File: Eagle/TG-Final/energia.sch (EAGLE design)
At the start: 55 parts, among them IC1 7812T, IC2 7805, IC3 AZ1117, IC4 7806T, Q1 TIP2955, T1 2N3904

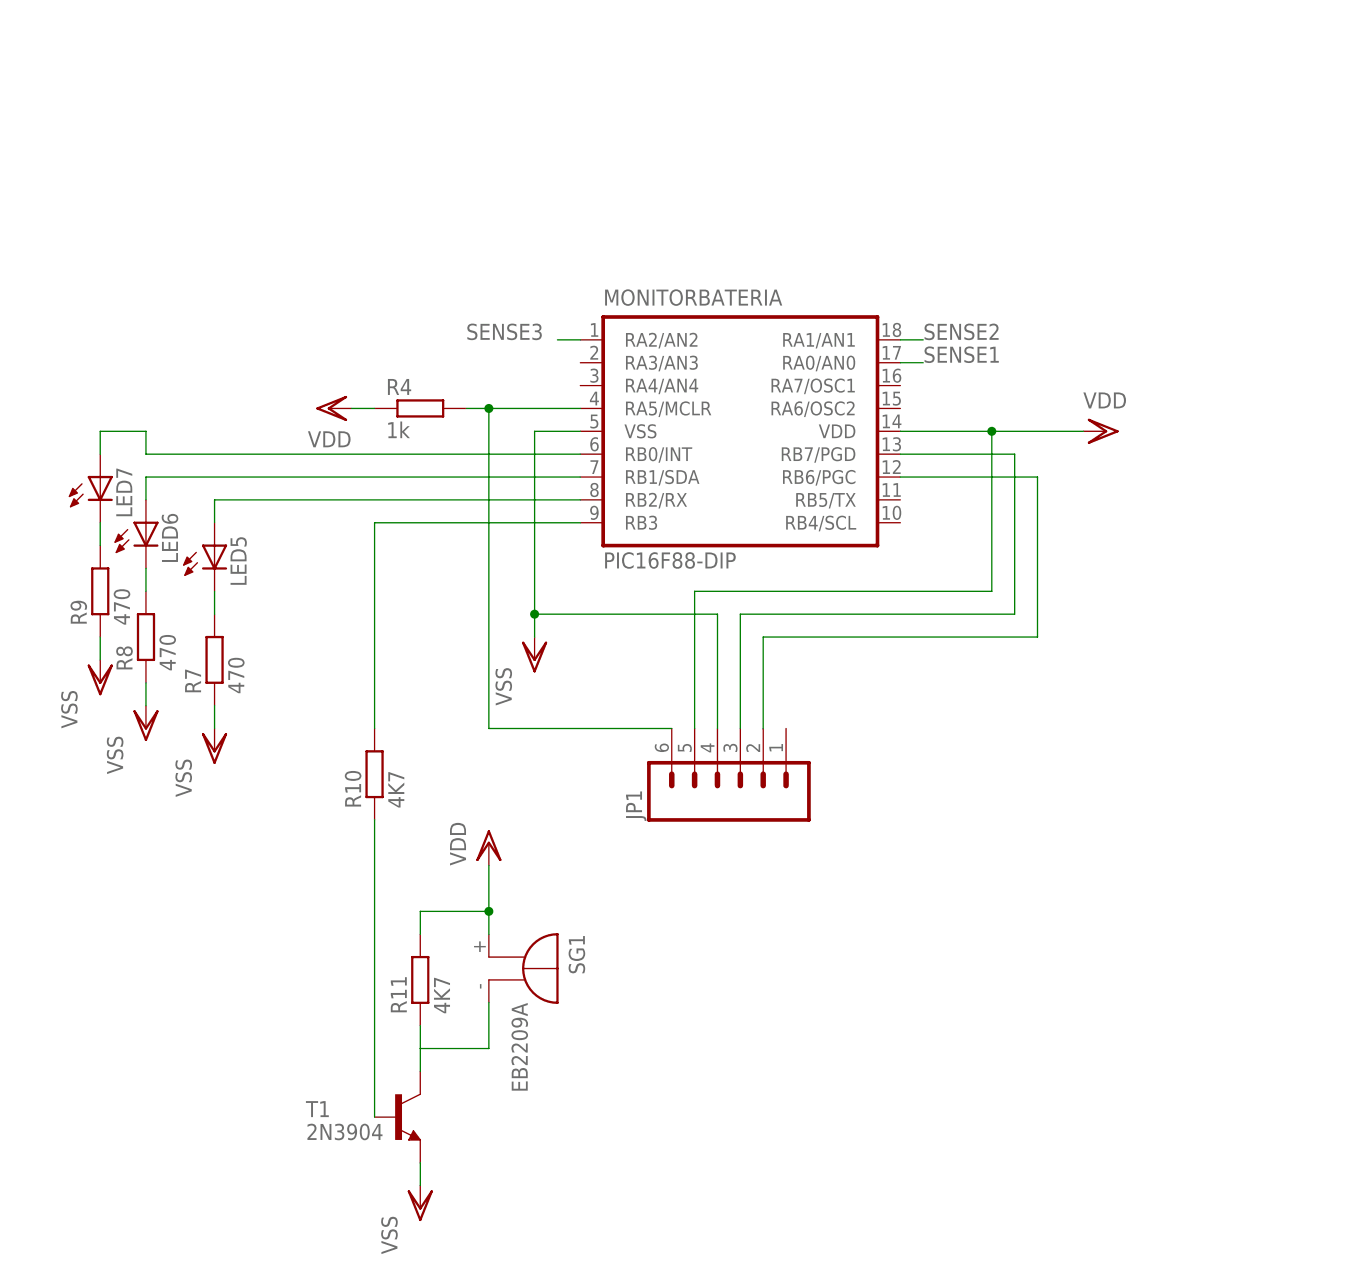
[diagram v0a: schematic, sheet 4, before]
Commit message: Placa Sub-Estación. Lista
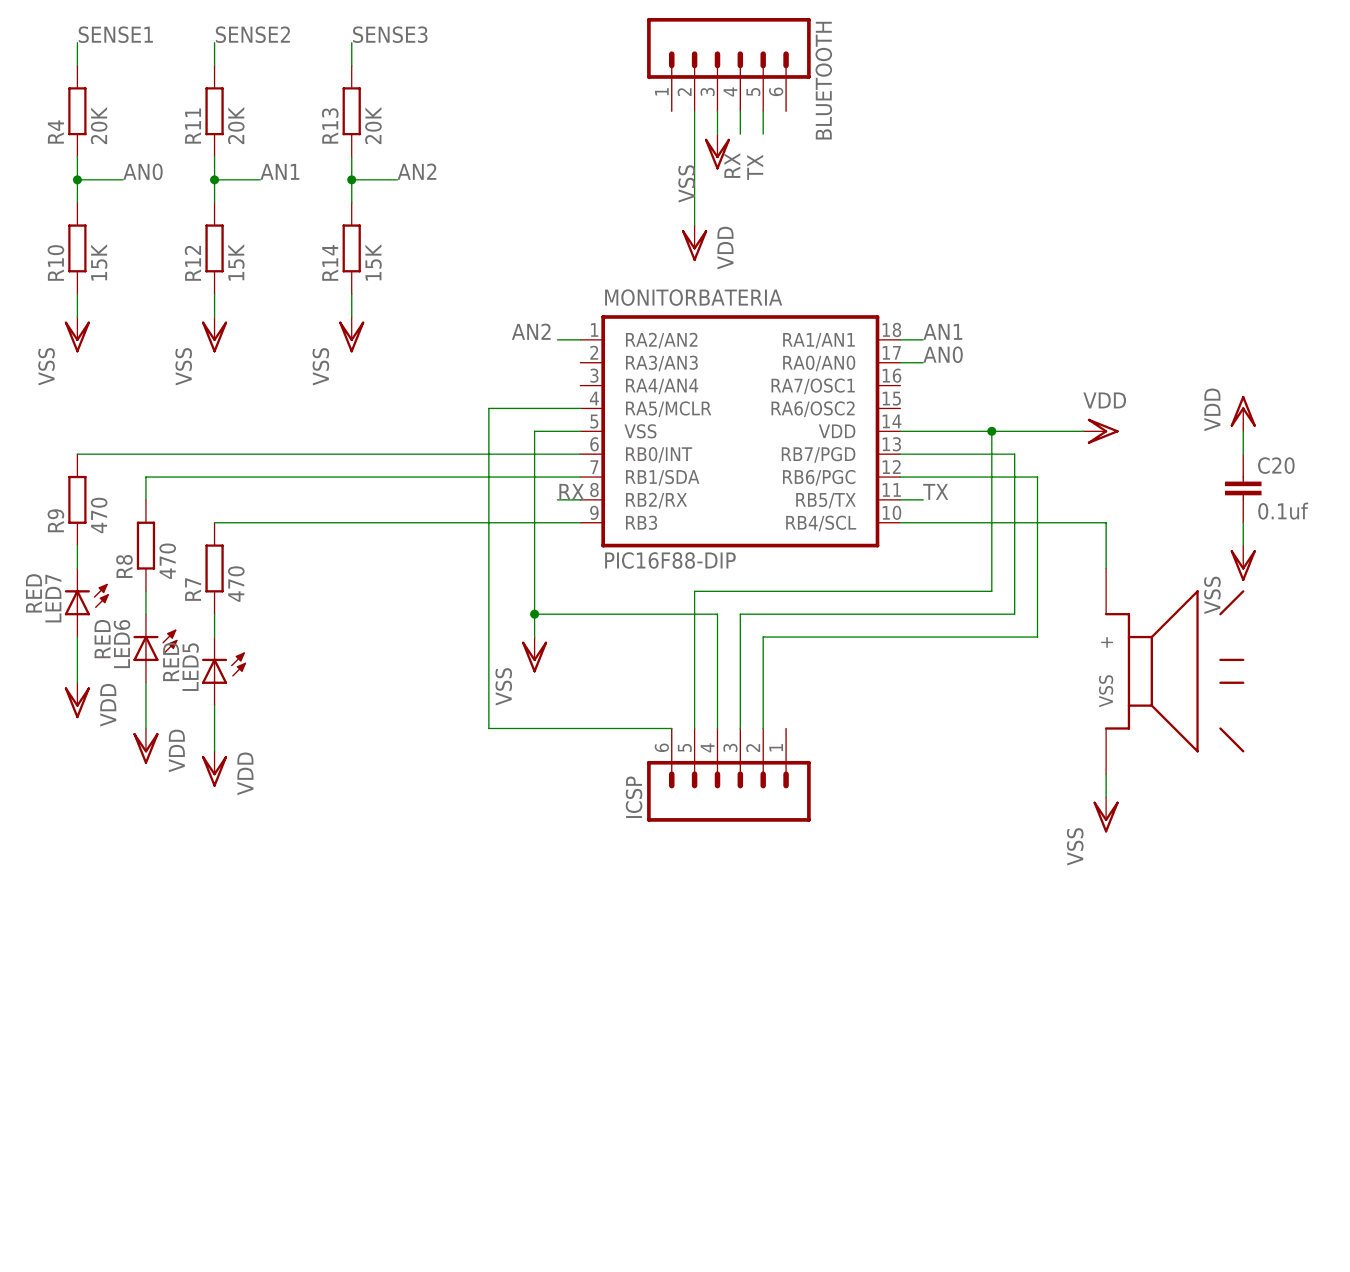
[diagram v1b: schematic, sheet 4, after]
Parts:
- removed SG1: EB2209A, buzzer:EB2209A
- removed T1: 2N3904, transistor:2N3904
- added BLUETOOTH: (no value), SparkFun:M06LONGPADS
- added C20: 0.1uf, rcl:C-EU050-024X044
- added R12, R14: 15K, rcl:R-EU_0204/5
- added R13: 20K, rcl:R-EU_0204/5
- added U$10: BUZZER, aasanchez:BUZZER
- LED5, LED6, LED7: value (none) -> RED
- R10: value 4K7 -> 15K; device rcl:R-EU_0207/10 -> rcl:R-EU_0204/5
- R11: value 4K7 -> 20K
- R4: value 1k -> 20K
- renumbered JP1 to ICSP
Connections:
- removed net N$23: MONITORBATERIA.RB3, R10.2
- removed net N$25: R11.1, SG1.-, T1.C
- new net AN0: MONITORBATERIA.RA0/AN0, R10.2, R4.1
- new net AN1: MONITORBATERIA.RA1/AN1, R11.1, R12.2
- new net AN2: MONITORBATERIA.RA2/AN2, R13.1, R14.2
- new net RX: BLUETOOTH.4, MONITORBATERIA.RB2/RX
- new net TX: BLUETOOTH.5, MONITORBATERIA.RB5/TX
- net N$15: now also R7.1; no longer R7.2
- net N$16: now also LED7.C, R9.1; no longer LED6.C, R8.2
- net N$19: now also LED6.C, R8.1; no longer LED7.C, R9.2
- net N$2: no longer R4.2
- net N$20: now also R9.2; no longer LED7.A
- net N$21: now also R8.2; no longer LED6.A
- net N$22: now also MONITORBATERIA.RB3, R7.2; no longer LED5.A, MONITORBATERIA.RB2/RX
- net N$24: now also MONITORBATERIA.RB4/SCL, U$10.+; no longer R10.1, T1.B
- net SENSE1: now also R4.2; no longer MONITORBATERIA.RA0/AN0
- net SENSE2: now also R11.2; no longer MONITORBATERIA.RA1/AN1
- net SENSE3: now also R13.2; no longer MONITORBATERIA.RA2/AN2
- net VDD: now also BLUETOOTH.2, C20.1, LED5.A, LED6.A, LED7.A; no longer R11.2, R4.1, SG1.+
- net VSS: now also BLUETOOTH.3, C20.2, R10.1, R12.1, R14.1, U$10.VSS; no longer R7.1, R8.1, R9.1, T1.E
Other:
- moved on the sheet: LED5, LED6, LED7, R10, R11, R4, R7, R8, R9

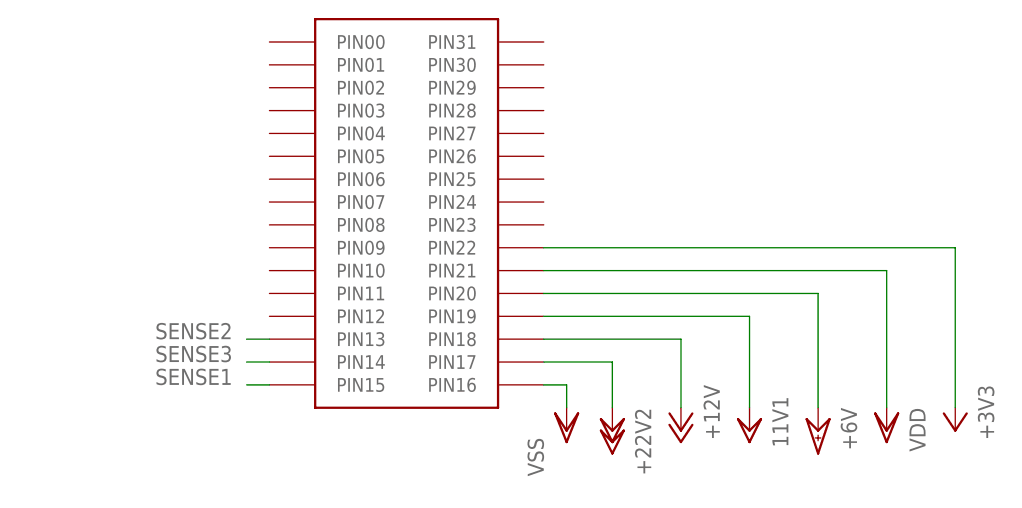
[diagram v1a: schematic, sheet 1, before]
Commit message: Placa de Control Motores y Comunicación
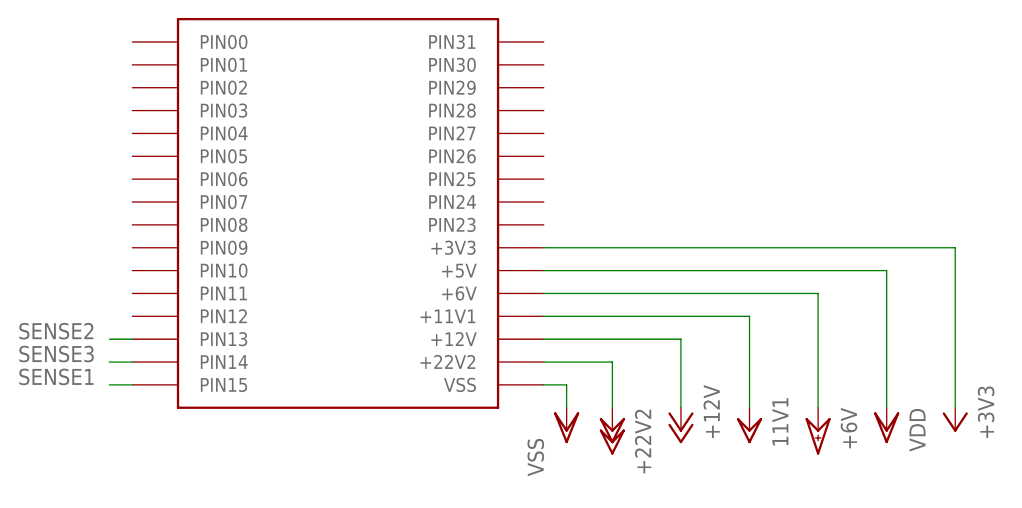
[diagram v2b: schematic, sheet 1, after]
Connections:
- net +11V1: now also U$1.+11V1; no longer U$1.PIN19
- net +12V: now also U$1.+12V; no longer U$1.PIN18
- net +22V: now also U$1.+22V2; no longer U$1.PIN17
- net +3V3: now also U$1.+3V3; no longer U$1.PIN22
- net +6V: now also U$1.+6V; no longer U$1.PIN20
- net VDD: now also U$1.+5V; no longer U$1.PIN21
- net VSS: now also U$1.VSS; no longer U$1.PIN16
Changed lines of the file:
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@@
 </plain>
 <instances>
-<instance part="U$1" gate="G$1" x="10.16" y="20.32"/>
+<instance part="U$1" gate="G$1" x="2.54" y="20.32"/>
 <instance part="VSS1" gate="G$1" x="27.94" y="-2.54"/>
 <instance part="U$2" gate="G$1" x="33.02" y="0" rot="R180"/>
@@
 <net name="VSS" class="0">
 <segment>
-<pinref part="U$1" gate="G$1" pin="PIN16"/>
+<pinref part="U$1" gate="G$1" pin="VSS"/>
 <pinref part="VSS1" gate="G$1" pin="VSS"/>
 <wire x1="25.4" y1="2.54" x2="27.94" y2="2.54" width="0.1524" layer="91"/>
@@
 <net name="+22V" class="0">
 <segment>
-<pinref part="U$1" gate="G$1" pin="PIN17"/>
+<pinref part="U$1" gate="G$1" pin="+22V2"/>
 <pinref part="U$2" gate="G$1" pin="+22V"/>
 <wire x1="25.4" y1="5.08" x2="33.02" y2="5.08" width="0.1524" layer="91"/>
@@
 <net name="+12V" class="0">
 <segment>
-<pinref part="U$1" gate="G$1" pin="PIN18"/>
+<pinref part="U$1" gate="G$1" pin="+12V"/>
 <pinref part="P+1" gate="1" pin="+12V"/>
 <wire x1="25.4" y1="7.62" x2="40.64" y2="7.62" width="0.1524" layer="91"/>
@@
 <net name="+11V1" class="0">
 <segment>
-<pinref part="U$1" gate="G$1" pin="PIN19"/>
+<pinref part="U$1" gate="G$1" pin="+11V1"/>
 <pinref part="U$3" gate="G$1" pin="+11V1"/>
 <wire x1="25.4" y1="10.16" x2="48.26" y2="10.16" width="0.1524" layer="91"/>
@@
 <net name="+6V" class="0">
 <segment>
-<pinref part="U$1" gate="G$1" pin="PIN20"/>
+<pinref part="U$1" gate="G$1" pin="+6V"/>
 <pinref part="U$4" gate="G$1" pin="+6V"/>
 <wire x1="25.4" y1="12.7" x2="55.88" y2="12.7" width="0.1524" layer="91"/>
@@
 <net name="+3V3" class="0">
 <segment>
-<pinref part="U$1" gate="G$1" pin="PIN22"/>
+<pinref part="U$1" gate="G$1" pin="+3V3"/>
 <pinref part="+3V1" gate="G$1" pin="+3V3"/>
 <wire x1="25.4" y1="17.78" x2="71.12" y2="17.78" width="0.1524" layer="91"/>
@@
 <net name="VDD" class="0">
 <segment>
-<pinref part="U$1" gate="G$1" pin="PIN21"/>
+<pinref part="U$1" gate="G$1" pin="+5V"/>
 <pinref part="VDD1" gate="G$1" pin="VDD"/>
 <wire x1="25.4" y1="15.24" x2="63.5" y2="15.24" width="0.1524" layer="91"/>
@@
 <segment>
 <pinref part="U$1" gate="G$1" pin="PIN15"/>
-<wire x1="-5.08" y1="2.54" x2="-7.62" y2="2.54" width="0.1524" layer="91"/>
-<label x="-17.78" y="2.54" size="1.778" layer="95"/>
+<wire x1="-20.32" y1="2.54" x2="-22.86" y2="2.54" width="0.1524" layer="91"/>
+<label x="-33.02" y="2.54" size="1.778" layer="95"/>
 </segment>
 </net>
@@
 <segment>
 <pinref part="U$1" gate="G$1" pin="PIN13"/>
-<wire x1="-5.08" y1="7.62" x2="-7.62" y2="7.62" width="0.1524" layer="91"/>
-<label x="-17.78" y="7.62" size="1.778" layer="95"/>
+<wire x1="-20.32" y1="7.62" x2="-22.86" y2="7.62" width="0.1524" layer="91"/>
+<label x="-33.02" y="7.62" size="1.778" layer="95"/>
 </segment>
 </net>
@@
 <segment>
 <pinref part="U$1" gate="G$1" pin="PIN14"/>
-<wire x1="-5.08" y1="5.08" x2="-7.62" y2="5.08" width="0.1524" layer="91"/>
-<label x="-17.78" y="5.08" size="1.778" layer="95"/>
+<wire x1="-20.32" y1="5.08" x2="-22.86" y2="5.08" width="0.1524" layer="91"/>
+<label x="-33.02" y="5.08" size="1.778" layer="95"/>
 </segment>
 </net>
